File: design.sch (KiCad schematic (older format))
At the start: 30 parts, among them J1 Conn_01x03

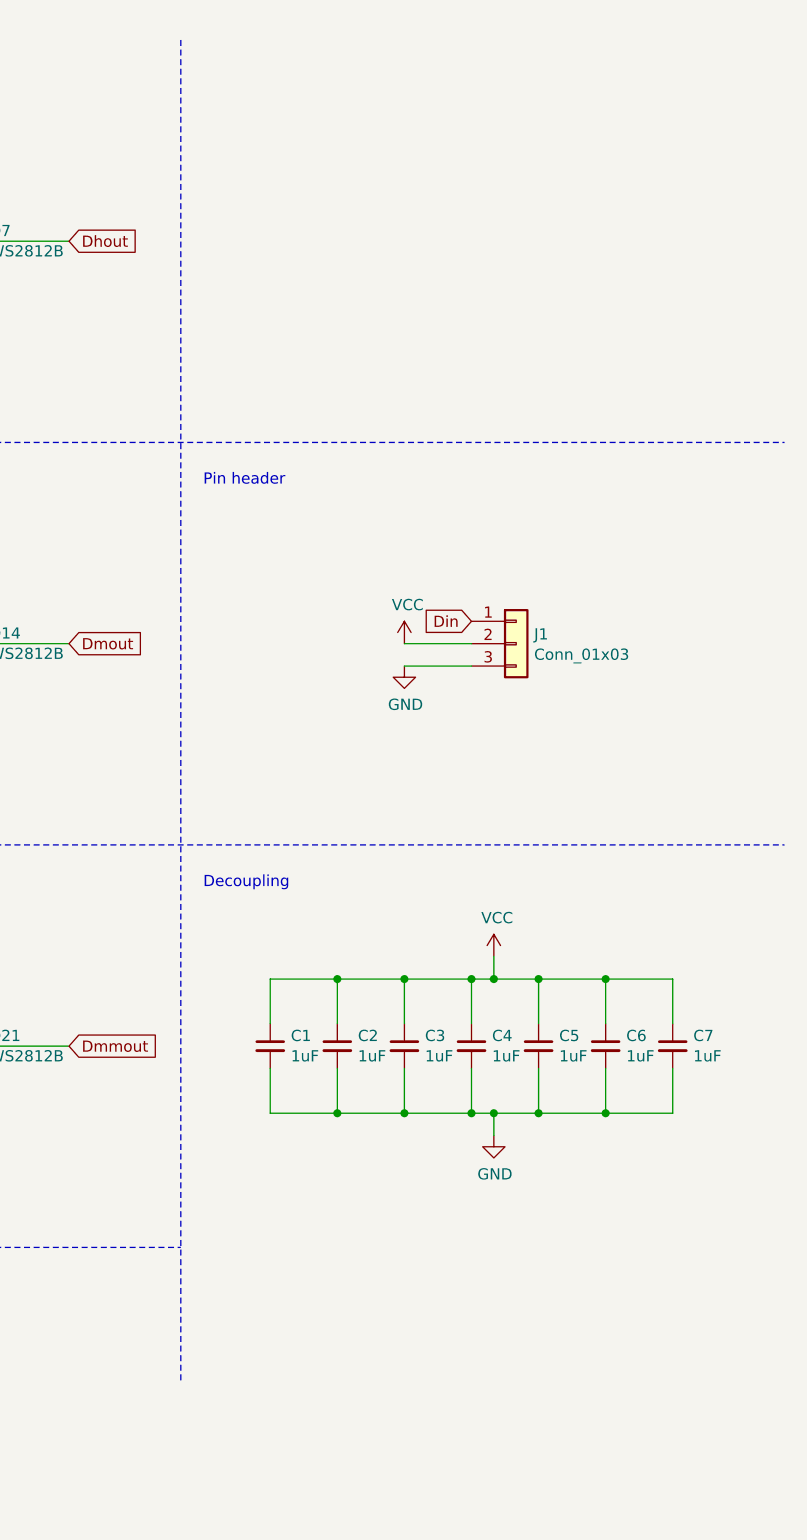
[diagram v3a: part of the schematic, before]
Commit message: added big capacitor and resistor @input
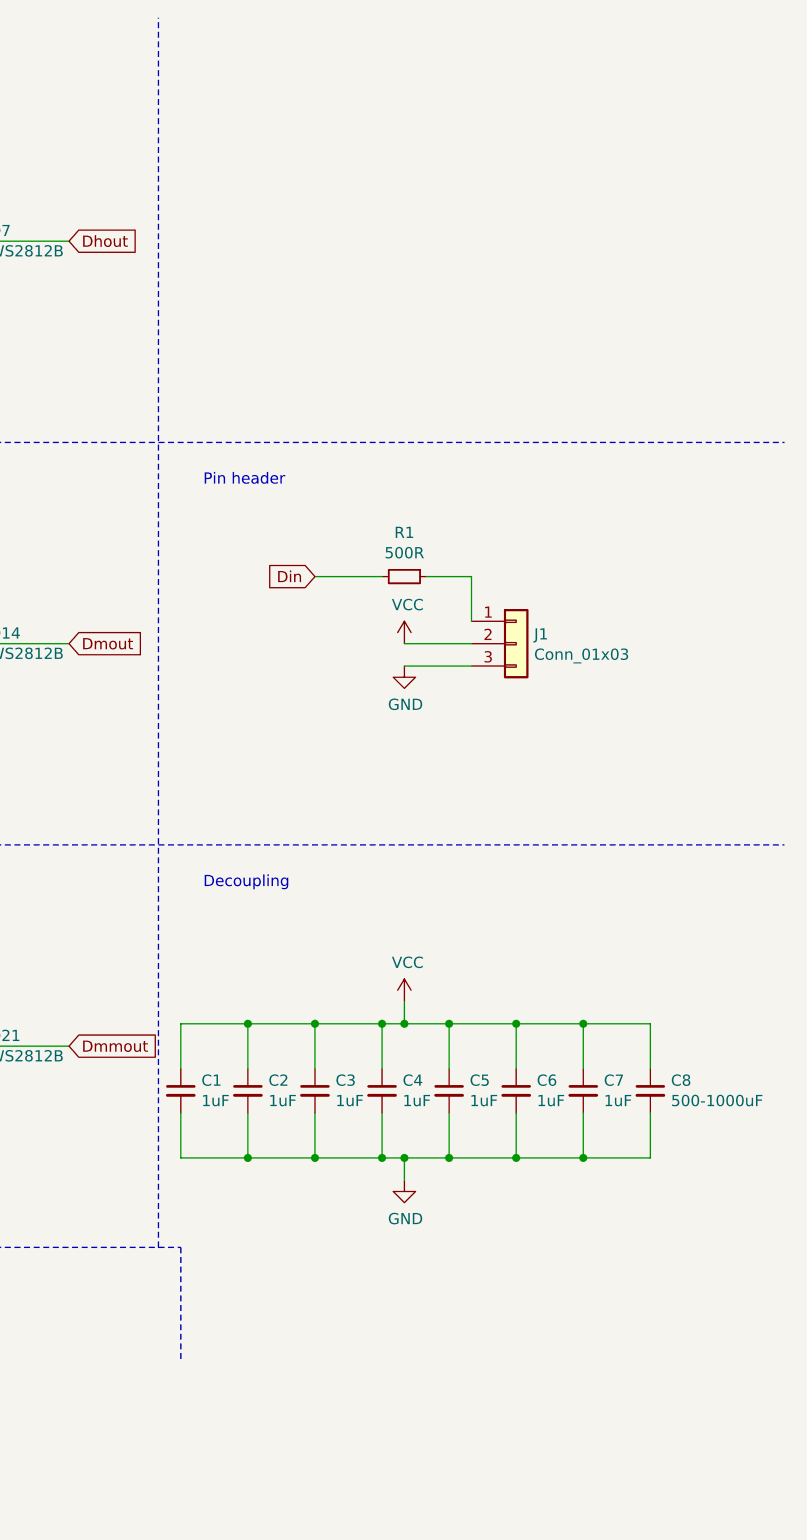
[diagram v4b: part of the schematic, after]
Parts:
- added C8: 500-1000uF, Capacitor_SMD:C_2225_5664Metric, symbol Device:C_Small
- added R1: 500R, Resistor_SMD:R_0805_2012Metric, symbol Device:R_Small
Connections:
- net Din: now also R1.2; no longer J1.1 (Pin_1)
- net GND: now also C8.2
- net VCC: now also C8.1
- new net: J1.1 (Pin_1), R1.1
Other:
- moved on the sheet: C1, C2, C3, C4, C5, C6, C7
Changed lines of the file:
@@
 Wire Wire Line
 	7600 5100 8000 5100
-Wire Notes Line
-	8500 600  8500 6600
 $Comp
 L LED:WS2812B D22
@@
 	1    0    0    -1
 $EndComp
-Text GLabel 9800 3200 0    50   Input ~ 0
+Text GLabel 9100 3000 0    50   Input ~ 0
 Din
 $Comp
@@
 L Device:C_Small C1
 U 1 1 61E06C0D
-P 8900 5100
-F 0 "C1" H 8992 5146 50  0000 L CNN
-F 1 "1uF" H 8992 5055 50  0000 L CNN
-F 2 "Capacitor_SMD:C_0805_2012Metric" H 8900 5100 50  0001 C CNN
-F 3 "~" H 8900 5100 50  0001 C CNN
-	1    8900 5100
-	1    0    0    -1
-$EndComp
-$Comp
-L Device:C_Small C2
-U 1 1 61E07C5C
-P 9200 5100
-F 0 "C2" H 9292 5146 50  0000 L CNN
-F 1 "1uF" H 9292 5055 50  0000 L CNN
-F 2 "Capacitor_SMD:C_0805_2012Metric" H 9200 5100 50  0001 C CNN
-F 3 "~" H 9200 5100 50  0001 C CNN
-	1    9200 5100
-	1    0    0    -1
-$EndComp
-$Comp
-L Device:C_Small C3
-U 1 1 61E0805D
-P 9500 5100
-F 0 "C3" H 9592 5146 50  0000 L CNN
-F 1 "1uF" H 9592 5055 50  0000 L CNN
-F 2 "Capacitor_SMD:C_0805_2012Metric" H 9500 5100 50  0001 C CNN
-F 3 "~" H 9500 5100 50  0001 C CNN
-	1    9500 5100
-	1    0    0    -1
-$EndComp
-$Comp
-L Device:C_Small C4
-U 1 1 61E08223
-P 9800 5100
-F 0 "C4" H 9892 5146 50  0000 L CNN
-F 1 "1uF" H 9892 5055 50  0000 L CNN
-F 2 "Capacitor_SMD:C_0805_2012Metric" H 9800 5100 50  0001 C CNN
-F 3 "~" H 9800 5100 50  0001 C CNN
-	1    9800 5100
-	1    0    0    -1
-$EndComp
-$Comp
-L Device:C_Small C5
-U 1 1 61E08809
-P 10100 5100
-F 0 "C5" H 10192 5146 50  0000 L CNN
-F 1 "1uF" H 10192 5055 50  0000 L CNN
-F 2 "Capacitor_SMD:C_0805_2012Metric" H 10100 5100 50  0001 C CNN
-F 3 "~" H 10100 5100 50  0001 C CNN
-	1    10100 5100
-	1    0    0    -1
-$EndComp
-$Comp
-L Device:C_Small C6
-U 1 1 61E08A0C
-P 10400 5100
-F 0 "C6" H 10492 5146 50  0000 L CNN
-F 1 "1uF" H 10492 5055 50  0000 L CNN
-F 2 "Capacitor_SMD:C_0805_2012Metric" H 10400 5100 50  0001 C CNN
-F 3 "~" H 10400 5100 50  0001 C CNN
-	1    10400 5100
-	1    0    0    -1
-$EndComp
-$Comp
-L Device:C_Small C7
-U 1 1 61E08FAF
-P 10700 5100
-F 0 "C7" H 10792 5146 50  0000 L CNN
-F 1 "1uF" H 10792 5055 50  0000 L CNN
-F 2 "Capacitor_SMD:C_0805_2012Metric" H 10700 5100 50  0001 C CNN
-F 3 "~" H 10700 5100 50  0001 C CNN
-	1    10700 5100
-	1    0    0    -1
-$EndComp
-$Comp
-L power:VCC #PWR031
-U 1 1 61E0B268
-P 9900 4700
-F 0 "#PWR031" H 9900 4550 50  0001 C CNN
-F 1 "VCC" H 9915 4873 50  0000 C CNN
-F 2 "" H 9900 4700 50  0001 C CNN
-F 3 "" H 9900 4700 50  0001 C CNN
-	1    9900 4700
-	1    0    0    -1
-$EndComp
-$Comp
-L power:GND #PWR046
-U 1 1 61E0BA4C
-P 9900 5500
-F 0 "#PWR046" H 9900 5250 50  0001 C CNN
-F 1 "GND" H 9905 5327 50  0000 C CNN
-F 2 "" H 9900 5500 50  0001 C CNN
-F 3 "" H 9900 5500 50  0001 C CNN
-	1    9900 5500
-	1    0    0    -1
-$EndComp
-Wire Wire Line
-	9900 4700 9900 4800
-Wire Wire Line
-	9900 4800 9800 4800
-Wire Wire Line
-	8900 4800 8900 5000
-Wire Wire Line
-	9200 5000 9200 4800
-Connection ~ 9200 4800
-Wire Wire Line
-	9200 4800 8900 4800
-Wire Wire Line
-	9500 5000 9500 4800
-Connection ~ 9500 4800
-Wire Wire Line
-	9500 4800 9200 4800
-Wire Wire Line
-	9900 4800 10100 4800
-Wire Wire Line
-	10700 4800 10700 5000
-Connection ~ 9900 4800
-Wire Wire Line
-	10400 5000 10400 4800
-Connection ~ 10400 4800
-Wire Wire Line
-	10400 4800 10700 4800
-Wire Wire Line
-	10100 5000 10100 4800
-Connection ~ 10100 4800
-Wire Wire Line
-	10100 4800 10400 4800
-Wire Wire Line
-	9800 5000 9800 4800
-Connection ~ 9800 4800
-Wire Wire Line
-	9800 4800 9500 4800
-Wire Wire Line
-	9900 5500 9900 5400
-Wire Wire Line
-	9900 5400 10100 5400
-Wire Wire Line
-	10700 5400 10700 5200
-Wire Wire Line
-	10400 5200 10400 5400
-Connection ~ 10400 5400
-Wire Wire Line
-	10400 5400 10700 5400
-Wire Wire Line
-	10100 5200 10100 5400
-Connection ~ 10100 5400
-Wire Wire Line
-	10100 5400 10400 5400
-Wire Wire Line
-	9900 5400 9800 5400
-Wire Wire Line
-	8900 5400 8900 5200
-Connection ~ 9900 5400
-Wire Wire Line
-	9200 5200 9200 5400
-Connection ~ 9200 5400
-Wire Wire Line
-	9200 5400 8900 5400
-Wire Wire Line
-	9500 5200 9500 5400
-Connection ~ 9500 5400
-Wire Wire Line
-	9500 5400 9200 5400
-Wire Wire Line
-	9800 5200 9800 5400
-Connection ~ 9800 5400
-Wire Wire Line
-	9800 5400 9500 5400
+P 8500 5300
+F 0 "C1" H 8592 5346 50  0000 L CNN
+F 1 "1uF" H 8592 5255 50  0000 L CNN
+F 2 "Capacitor_SMD:C_0805_2012Metric" H 8500 5300 50  0001 C CNN
+F 3 "~" H 8500 5300 50  0001 C CNN
+	1    8500 5300
+	1    0    0    -1
+$EndComp
+Wire Wire Line
+	8500 5000 8500 5200
+Wire Wire Line
+	8500 5600 8500 5400
 Wire Notes Line
 	500  4200 11200 4200
@@
 Wire Notes Line
 	500  6000 8500 6000
+Wire Notes Line
+	8400 6000 8400 500
+Wire Notes Line
+	8500 6000 8500 6500
+Connection ~ 10300 5600
+Wire Wire Line
+	10600 5600 10300 5600
+Wire Wire Line
+	10600 5400 10600 5600
+Connection ~ 10300 5000
+Wire Wire Line
+	10600 5000 10600 5200
+Wire Wire Line
+	10300 5000 10600 5000
+$Comp
+L Device:C_Small C8
+U 1 1 61DB3592
+P 10600 5300
+F 0 "C8" H 10692 5346 50  0000 L CNN
+F 1 "500-1000uF" H 10692 5255 50  0000 L CNN
+F 2 "Capacitor_SMD:C_2225_5664Metric" H 10600 5300 50  0001 C CNN
+F 3 "~" H 10600 5300 50  0001 C CNN
+	1    10600 5300
+	1    0    0    -1
+$EndComp
+Wire Wire Line
+	9400 5600 9100 5600
+Connection ~ 9400 5600
+Wire Wire Line
+	9400 5400 9400 5600
+Wire Wire Line
+	9100 5600 8800 5600
+Connection ~ 9100 5600
+Wire Wire Line
+	9100 5400 9100 5600
+Wire Wire Line
+	8800 5600 8500 5600
+Connection ~ 8800 5600
+Wire Wire Line
+	8800 5400 8800 5600
+Connection ~ 9500 5600
+Wire Wire Line
+	9500 5600 9400 5600
+Wire Wire Line
+	9700 5600 10000 5600
+Connection ~ 9700 5600
+Wire Wire Line
+	9700 5400 9700 5600
+Wire Wire Line
+	10000 5600 10300 5600
+Connection ~ 10000 5600
+Wire Wire Line
+	10000 5400 10000 5600
+Wire Wire Line
+	10300 5600 10300 5400
+Wire Wire Line
+	9500 5600 9700 5600
+Wire Wire Line
+	9500 5700 9500 5600
+Wire Wire Line
+	9400 5000 9100 5000
+Connection ~ 9400 5000
+Wire Wire Line
+	9400 5200 9400 5000
+Wire Wire Line
+	9700 5000 10000 5000
+Connection ~ 9700 5000
+Wire Wire Line
+	9700 5200 9700 5000
+Wire Wire Line
+	10000 5000 10300 5000
+Connection ~ 10000 5000
+Wire Wire Line
+	10000 5200 10000 5000
+Connection ~ 9500 5000
+Wire Wire Line
+	10300 5000 10300 5200
+Wire Wire Line
+	9500 5000 9700 5000
+Wire Wire Line
+	9100 5000 8800 5000
+Connection ~ 9100 5000
+Wire Wire Line
+	9100 5200 9100 5000
+Wire Wire Line
+	8800 5000 8500 5000
+Connection ~ 8800 5000
+Wire Wire Line
+	8800 5200 8800 5000
+Wire Wire Line
+	9500 5000 9400 5000
+Wire Wire Line
+	9500 4900 9500 5000
+$Comp
+L power:GND #PWR046
+U 1 1 61E0BA4C
+P 9500 5700
+F 0 "#PWR046" H 9500 5450 50  0001 C CNN
+F 1 "GND" H 9505 5527 50  0000 C CNN
+F 2 "" H 9500 5700 50  0001 C CNN
+F 3 "" H 9500 5700 50  0001 C CNN
+	1    9500 5700
+	1    0    0    -1
+$EndComp
+$Comp
+L power:VCC #PWR031
+U 1 1 61E0B268
+P 9500 4900
+F 0 "#PWR031" H 9500 4750 50  0001 C CNN
+F 1 "VCC" H 9515 5073 50  0000 C CNN
+F 2 "" H 9500 4900 50  0001 C CNN
+F 3 "" H 9500 4900 50  0001 C CNN
+	1    9500 4900
+	1    0    0    -1
+$EndComp
+$Comp
+L Device:C_Small C7
+U 1 1 61E08FAF
+P 10300 5300
+F 0 "C7" H 10392 5346 50  0000 L CNN
+F 1 "1uF" H 10392 5255 50  0000 L CNN
+F 2 "Capacitor_SMD:C_0805_2012Metric" H 10300 5300 50  0001 C CNN
+F 3 "~" H 10300 5300 50  0001 C CNN
+	1    10300 5300
+	1    0    0    -1
+$EndComp
+$Comp
+L Device:C_Small C6
+U 1 1 61E08A0C
+P 10000 5300
+F 0 "C6" H 10092 5346 50  0000 L CNN
+F 1 "1uF" H 10092 5255 50  0000 L CNN
+F 2 "Capacitor_SMD:C_0805_2012Metric" H 10000 5300 50  0001 C CNN
+F 3 "~" H 10000 5300 50  0001 C CNN
+	1    10000 5300
+	1    0    0    -1
+$EndComp
+$Comp
+L Device:C_Small C5
+U 1 1 61E08809
+P 9700 5300
+F 0 "C5" H 9792 5346 50  0000 L CNN
+F 1 "1uF" H 9792 5255 50  0000 L CNN
+F 2 "Capacitor_SMD:C_0805_2012Metric" H 9700 5300 50  0001 C CNN
+F 3 "~" H 9700 5300 50  0001 C CNN
+	1    9700 5300
+	1    0    0    -1
+$EndComp
+$Comp
+L Device:C_Small C4
+U 1 1 61E08223
+P 9400 5300
+F 0 "C4" H 9492 5346 50  0000 L CNN
+F 1 "1uF" H 9492 5255 50  0000 L CNN
+F 2 "Capacitor_SMD:C_0805_2012Metric" H 9400 5300 50  0001 C CNN
+F 3 "~" H 9400 5300 50  0001 C CNN
+	1    9400 5300
+	1    0    0    -1
+$EndComp
+$Comp
+L Device:C_Small C3
+U 1 1 61E0805D
+P 9100 5300
+F 0 "C3" H 9192 5346 50  0000 L CNN
+F 1 "1uF" H 9192 5255 50  0000 L CNN
+F 2 "Capacitor_SMD:C_0805_2012Metric" H 9100 5300 50  0001 C CNN
+F 3 "~" H 9100 5300 50  0001 C CNN
+	1    9100 5300
+	1    0    0    -1
+$EndComp
+$Comp
+L Device:C_Small C2
+U 1 1 61E07C5C
+P 8800 5300
+F 0 "C2" H 8892 5346 50  0000 L CNN
+F 1 "1uF" H 8892 5255 50  0000 L CNN
+F 2 "Capacitor_SMD:C_0805_2012Metric" H 8800 5300 50  0001 C CNN
+F 3 "~" H 8800 5300 50  0001 C CNN
+	1    8800 5300
+	1    0    0    -1
+$EndComp
+$Comp
+L Device:R_Small R1
+U 1 1 61DE3374
+P 9500 3000
+F 0 "R1" V 9304 3000 50  0000 C CNN
+F 1 "500R" V 9395 3000 50  0000 C CNN
+F 2 "Resistor_SMD:R_0805_2012Metric" H 9500 3000 50  0001 C CNN
+F 3 "~" H 9500 3000 50  0001 C CNN
+	1    9500 3000
+	0    1    1    0
+$EndComp
+Wire Wire Line
+	9600 3000 9800 3000
+Wire Wire Line
+	9800 3000 9800 3200
+Wire Wire Line
+	9400 3000 9100 3000
 $EndSCHEMATC
